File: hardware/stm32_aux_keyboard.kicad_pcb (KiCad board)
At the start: 2 copper layers, 95 x 95 mm, 189 parts, among them J1 I2C_HEADER,2.54, J2 WS2812_HEADER, J3 BUZZER_HEADER, J4 ROT_ENC_HEADER, J5 SWD_SWD, J6 SWD_SWD, J7 ROT_ENC_HEADER, J8 I2C_HEADER,2.54, Q1 SS9013_J3, SW1 USR_BTN_1, SW10 KEY22, SW11 KEY23, SW12 KEY31, SW13 KEY32, SW14 KEY33, SW18 ROT1, SW19 SW_RESET,2_leg,SMD, SW2 USR_BTN_2, SW3 USR_BTN_3, SW5 ROT2, SW6 KEY11, SW7 KEY12, SW8 KEY13, SW9 KEY21, U1 SSD1306-OLED-I2C, U10 STM32F103C8T6, U2 AMS1117-3.3, U3 74AHCT1G125, U4 USB, U5 USBLC6-2SC6_SOT23-6, U6 STM32F103C8T6_rect, U7 SWD, U8 AMS1117-3.3, U9 USBLC6-2SC6_SOT23-6, Y1 O_8M, Y2 O8M, Y3 O32.768K

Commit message: update,
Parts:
- removed REF**: test1, casing:test1
- JP7: value B0 -> BOOT0
- JP8: value B1 -> BOOT1
- U5, U9: moved to F.Cu
- moved J1 8.20 mm to (99.2, 99.4)
- moved U9 7.69 mm to (82.3, 28.1), turned to 90 degrees
- moved RN4 7.02 mm to (82.6, 29.6), turned to 270 degrees
- moved R2 4.70 mm to (104.0, 95.7), turned to 270 degrees
- moved U5 4.69 mm to (88.2, 29.5), turned to 270 degrees
- moved TP8 2.70 mm to (85.8, 32.5)
- moved R1 2.30 mm to (106.0, 95.7), turned to 270 degrees
- renumbered VUSB1 to VUSB1_HEALTHY1
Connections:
- RN4 pad 1: Net-(RN4-Pad1) -> Net-(R27-Pad2)
- RN4 pad 2: Net-(R27-Pad2) -> Net-(RN4-Pad2)
- RN4 pad 7: /stm32_swd/USB_P -> /stm32_swd/USB_N
- RN4 pad 8: /stm32_swd/USB_N -> /stm32_swd/USB_P
- U9 pad 4: Net-(RN4-Pad1) -> Net-(RN4-Pad2)
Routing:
- net Vusb: track 44.9 -> 14.2 mm, vias 4 -> 3
- net /oled/SCL: track 108.4 -> 86.2 mm, vias 1 -> 4
- net /oled/SDA: track 77.6 -> 88.6 mm, vias 3 -> 4
- net Net-(RN4-Pad1): track 9.28 -> 0.99 mm
- net Net-(U7-Pad3): track 19.2 -> 11.5 mm, vias 1 -> 2
- net /stm32_swd/USB_P: track 59.8 -> 52.8 mm, vias 3 -> 1
- net /stm32_core/USR_BTN3: track 90.8 -> 97.0 mm
- net Voled: track 36.7 -> 41.9 mm
- net Net-(RN1-Pad1): track 11.7 -> 6.92 mm, vias 1 -> 0
- net /stm32_swd/USB_N: track 55.2 -> 50.5 mm, vias 3 -> 1
- net Net-(JP8-Pad2): track 35.7 -> 31.8 mm
- net VCC: track 407.5 -> 411.2 mm
- net Net-(RN4-Pad2): track 0.00 -> 3.50 mm, vias 0 -> 1
- net Net-(U7-Pad2): track 15.2 -> 12.2 mm, vias 1 -> 2
- net Net-(RN1-Pad2): track 8.24 -> 11.1 mm, vias 1 -> 0
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
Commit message: update,
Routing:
- net GND: track 984.0 -> 990.1 mm
- net VCC: track 411.2 -> 406.6 mm, vias 8 -> 9
- net Net-(R27-Pad2): track 12.2 -> 15.5 mm, vias 1 -> 2
- net Vstm32_stlink: track 172.1 -> 172.9 mm

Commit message: update,
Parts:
- JP5, JP6, R25, R5, R6: moved to B.Cu
- moved RN1 6.00 mm to (91.9, 29.1), turned to 0 degrees
- moved R25 4.63 mm to (93.5, 32.1), turned to 180 degrees
- moved R22 4.17 mm to (103.0, 36.0), turned to 0 degrees
- moved R23 4.06 mm to (103.0, 34.0), turned to 180 degrees
- moved JP6 4.00 mm to (109.1, 36.4)
- moved JP5 3.93 mm to (106.5, 36.4)
- moved R26 3.76 mm to (74.4, 25.4)
- moved C31 3.10 mm to (98.9, 40.7)
- moved C32 3.10 mm to (96.9, 44.7)
- moved C33 3.10 mm to (96.9, 47.7)
- moved C34 3.10 mm to (105.4, 42.7)
- moved C35 3.10 mm to (103.7, 49.2)
- moved R19 3.10 mm to (96.9, 43.2)
- moved R20 3.10 mm to (100.9, 40.7)
- moved R21 3.10 mm to (96.9, 46.2)
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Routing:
- net /stm32_core/USB_P: track 76.7 -> 141.7 mm, vias 4 -> 2
- net Vusb: track 14.2 -> 48.6 mm, vias 3 -> 5
- net /stm32_swd/T_JTMS: track 19.8 -> 53.4 mm, vias 1 -> 5
- net GND: track 990.1 -> 963.2 mm, vias 9 -> 12
- net /stm32_swd/T_JTCK: track 19.2 -> 40.4 mm, vias 1 -> 3
- net /stm32_swd/D_SWDIO: track 62.7 -> 83.6 mm, vias 1 -> 2
- net /stm32_swd/USB_N: track 50.5 -> 65.4 mm, vias 1 -> 3
- net /stm32_swd/D_SWCLK: track 51.1 -> 65.0 mm, vias 1 -> 3
- net Net-(D25-Pad1): track 13.5 -> 3.47 mm
- net /oled/SCL: track 86.2 -> 94.7 mm, vias 4 -> 5
- net /oled/SDA: track 88.6 -> 80.1 mm, vias 4 -> 5
- net /keyboard_key/COL3: track 79.8 -> 88.0 mm, vias 3 -> 5
- net /stm32_swd/USB_P: track 52.8 -> 45.1 mm, vias 1 -> 3
- net Net-(RN1-Pad2): track 11.1 -> 3.53 mm
- net Vstm32_stlink: track 172.9 -> 165.5 mm
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
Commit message: update for autoroute complete,
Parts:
- moved R23 1.50 mm to (103.1, 32.5)
- moved JP6 1.10 mm to (110.2, 36.5)
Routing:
- net GND: track 963.2 -> 885.7 mm, vias 12 -> 5
- net /stm32_core/USB_P: track 141.7 -> 70.4 mm, vias 2 -> 0
- net /stm32_core/BOOT1: track 81.2 -> 22.3 mm, vias 0 -> 2
- net /status_display/USR_LED_2: track 101.2 -> 150.1 mm, vias 4 -> 0
- net /status_display/USR_LED_1: track 88.8 -> 130.5 mm, vias 2 -> 0
- net /keyboard_key/ROW2: track 86.6 -> 125.4 mm
- net /stm32_swd/T_JTMS: track 53.4 -> 18.4 mm, vias 5 -> 1
- net /stm32_swd/USB_N: track 65.4 -> 34.0 mm, vias 3 -> 1
- net /stm32_swd/T_JTCK: track 40.4 -> 12.5 mm, vias 3 -> 1
- net /stm32_core/USB_N: track 79.5 -> 54.3 mm, vias 3 -> 2
- net /oled/SCL: track 94.7 -> 72.9 mm, vias 5 -> 0
- net VCC: track 409.2 -> 387.6 mm, vias 9 -> 6
- net /WS2812/WS2812_IN: track 170.4 -> 191.4 mm, vias 2 -> 1
- net /stm32_core/PC13: track 29.3 -> 9.72 mm
- net +3V3: track 249.7 -> 269.1 mm, vias 3 -> 1
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
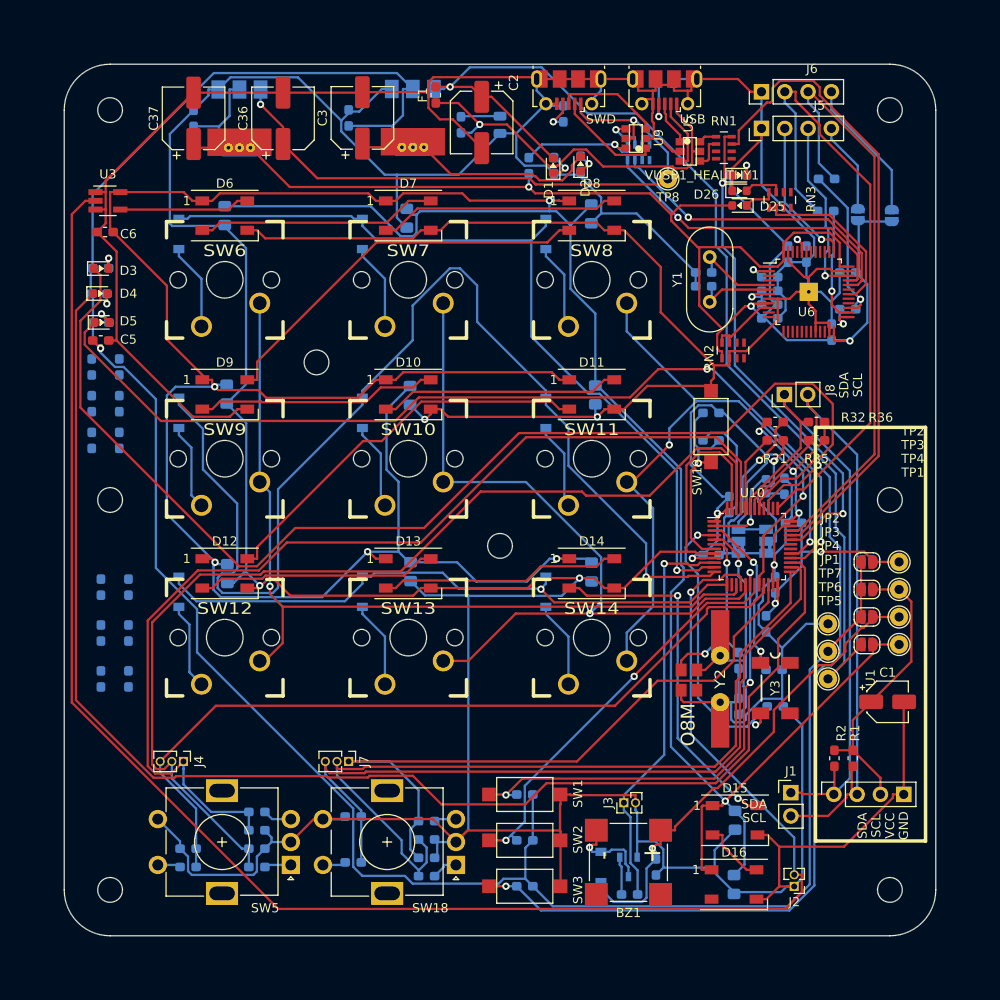
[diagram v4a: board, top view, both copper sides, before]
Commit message: update for tidy tracks,
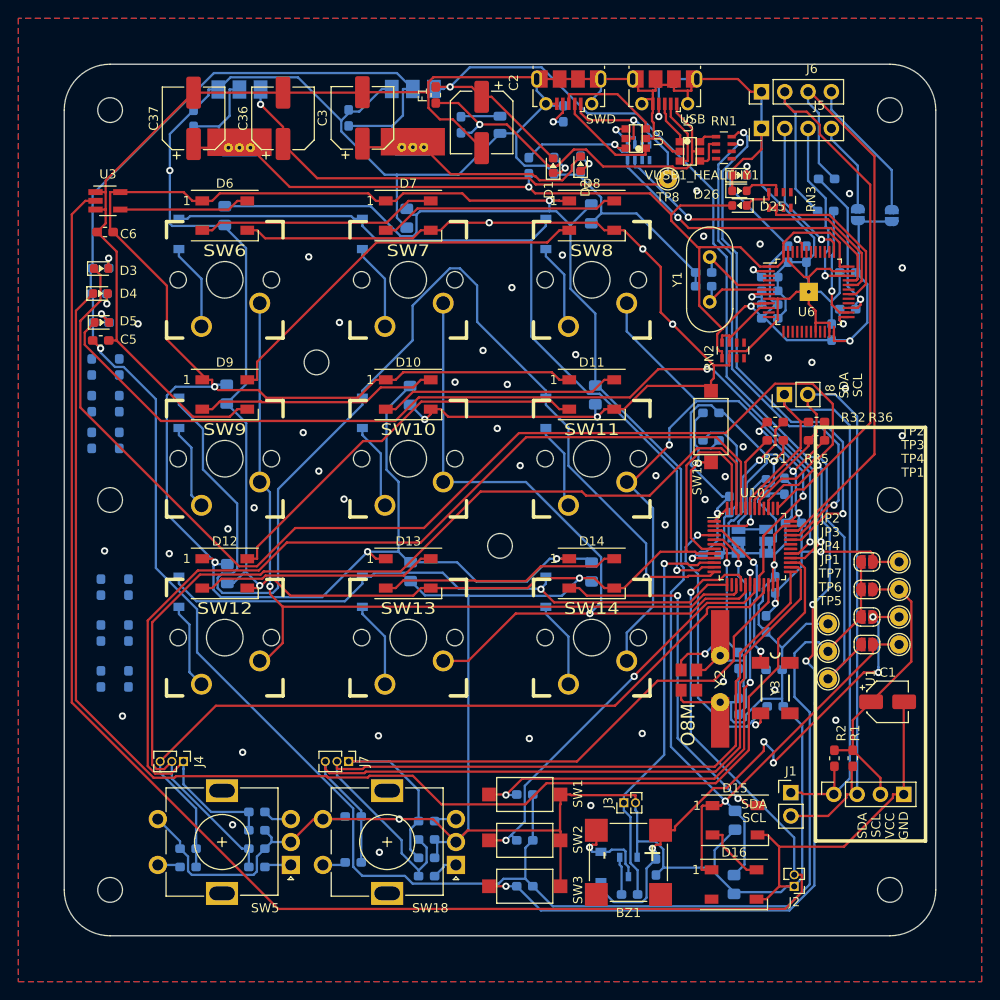
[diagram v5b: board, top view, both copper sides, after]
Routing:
- net /stm32_core/USB_P: track 70.4 -> 55.2 mm, vias 0 -> 2
- net Vbuzzer: track 52.9 -> 58.6 mm, vias 1 -> 5
- net /stm32_core/USB_N: track 54.3 -> 58.6 mm
- net +3V3: track 269.1 -> 273.3 mm
- net /oled/SDA: track 71.4 -> 74.3 mm
- net /oled/SCL: track 72.9 -> 74.7 mm
- net +5V: track 118.2 -> 118.9 mm
- net /stm32_core/USR_BTN3: track 94.0 -> 93.4 mm, vias 2 -> 4
- net GND: track 885.7 -> 886.2 mm, vias 5 -> 53
- added copper zone on B.Cu, net GND
- added copper zone on F.Cu, net GND

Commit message: update for tidy tracks,
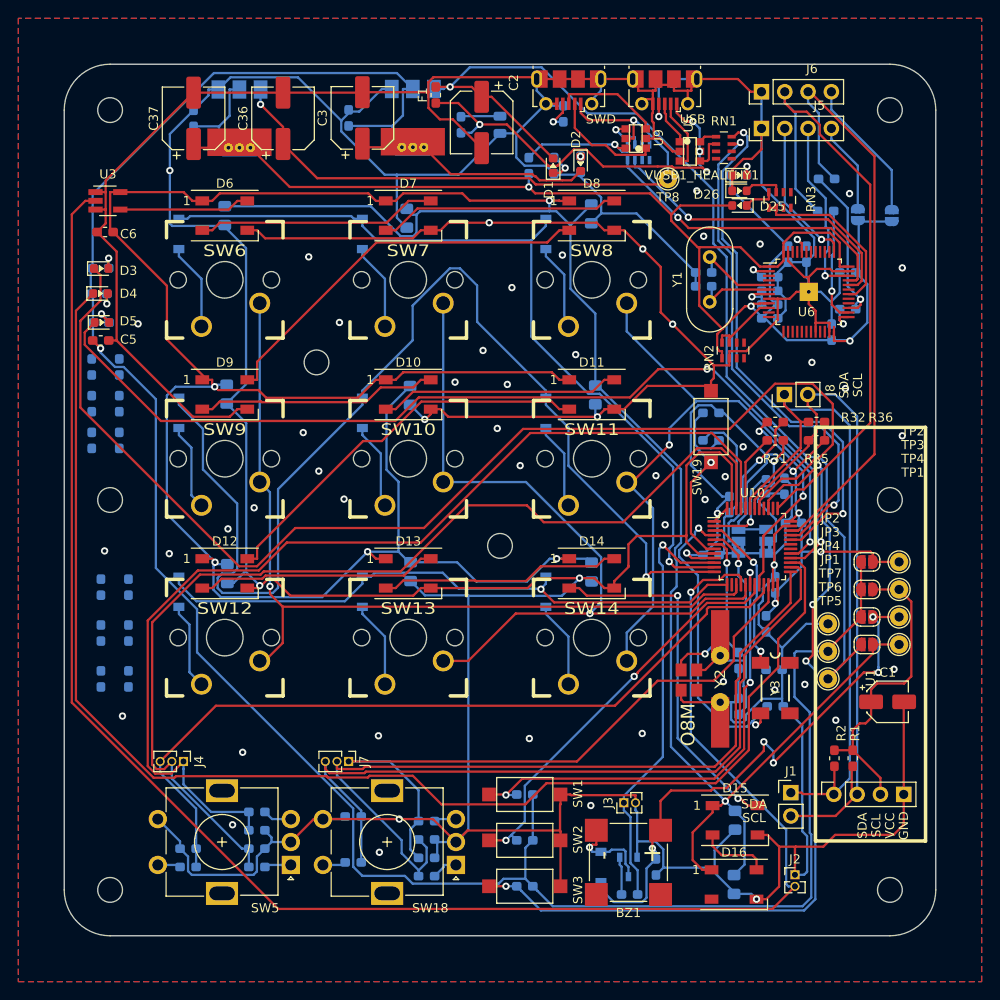
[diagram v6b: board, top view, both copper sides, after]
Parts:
- moved J2 1.27 mm to (99.7, 108.3), turned to 0 degrees
- turned D2 to 270 degrees
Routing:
- net /stm32_core/BUZZER: track 44.1 -> 47.2 mm
- net Vusb: track 43.0 -> 45.8 mm, vias 1 -> 4
- net Net-(D2-Pad1): track 2.47 -> 0.00 mm
- net Voled: track 31.6 -> 33.7 mm
- net /stm32_core/OSC32K_N: track 32.5 -> 34.1 mm
- net Vstm32: track 91.4 -> 92.8 mm
- net Vbuzzer: track 58.6 -> 59.9 mm
- net /rot_enc2/B: track 111.1 -> 112.3 mm
- net /WS2812/WS2812_IN: track 191.4 -> 190.3 mm
- net /stm32_core/USR_BTN3: track 93.4 -> 94.4 mm
- net Net-(U7-Pad2): track 11.4 -> 12.3 mm
- net +3V3: track 273.3 -> 272.5 mm
- net GND: track 886.2 -> 886.9 mm, vias 53 -> 56
- net Net-(D15-Pad2): track 7.04 -> 7.75 mm
- net /stm32_core/RESET: track 21.5 -> 21.0 mm

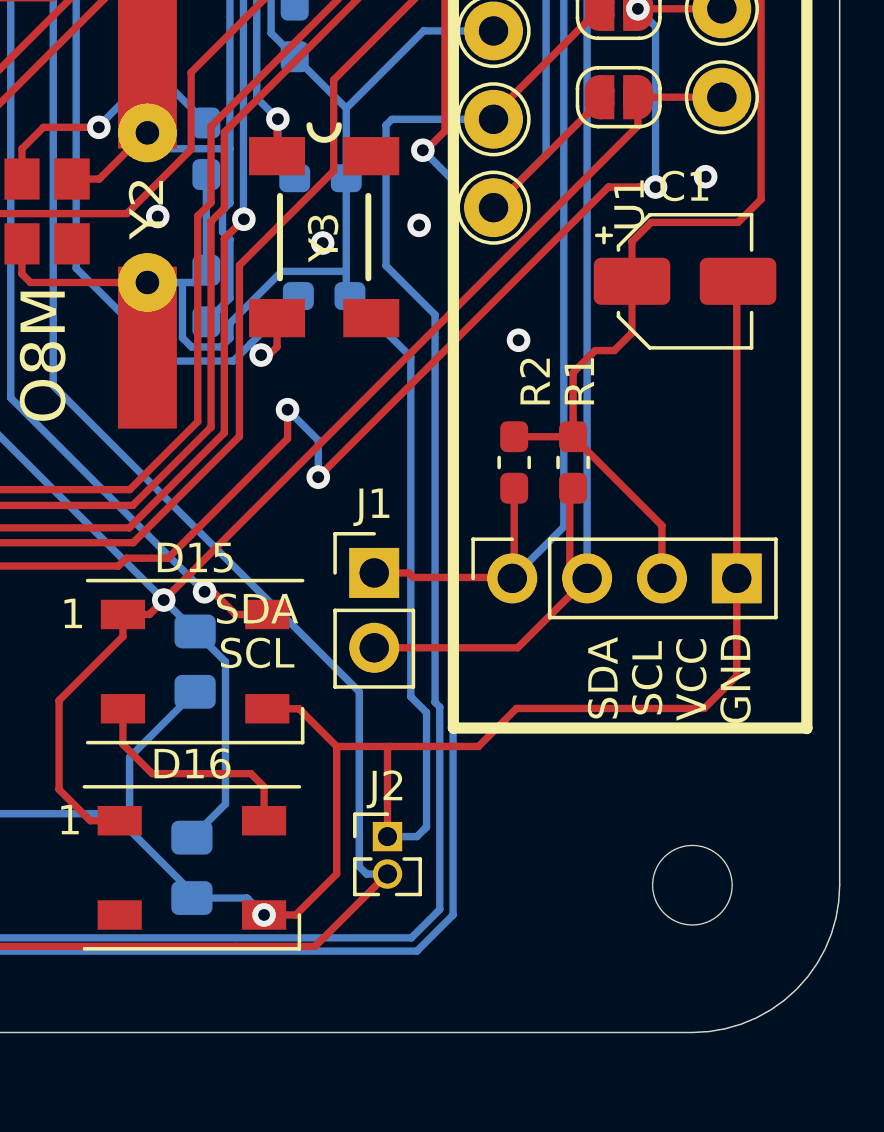
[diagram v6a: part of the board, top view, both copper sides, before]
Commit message: update for tidy tracks,
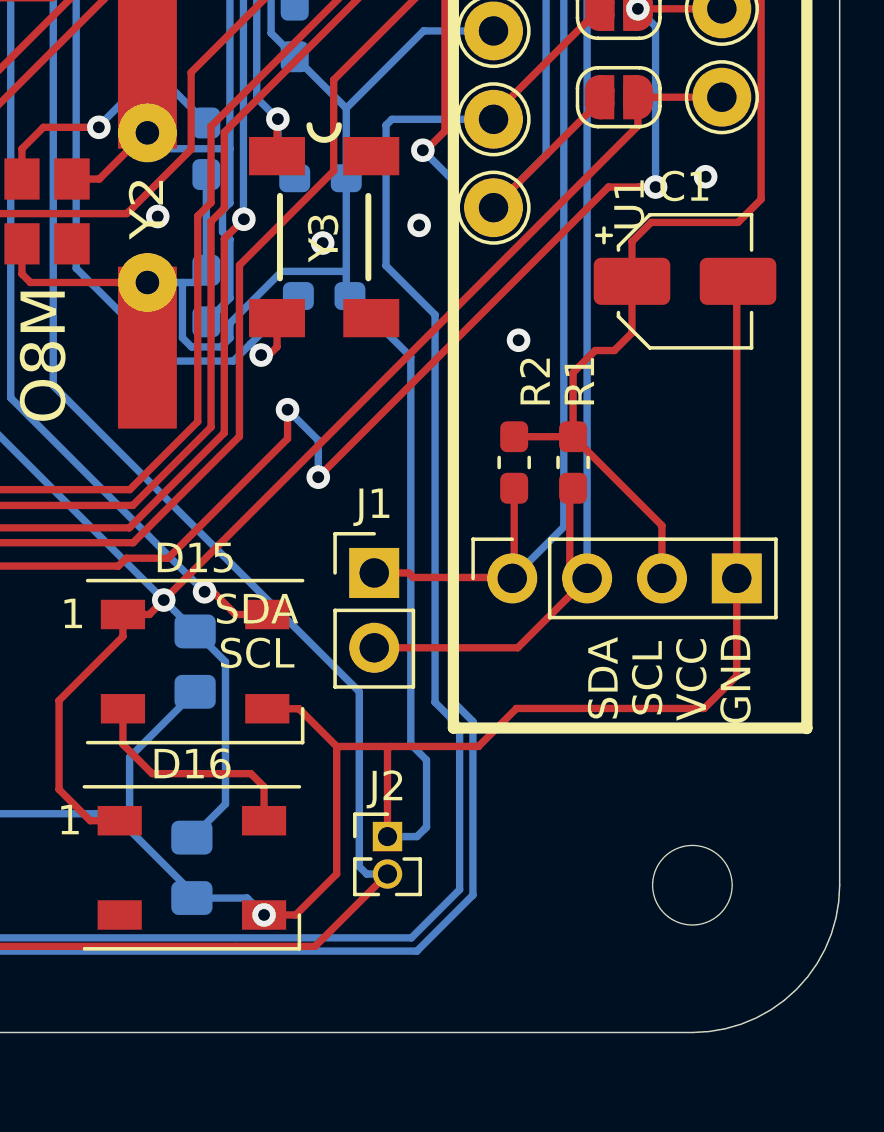
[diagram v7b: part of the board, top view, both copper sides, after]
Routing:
- net +3V3: track 272.5 -> 273.1 mm
- net /stm32_core/USR_BTN3: track 94.4 -> 95.0 mm
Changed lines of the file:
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@@
     (thickness 1.6)
     (drawings 18)
-    (tracks 1801)
+    (tracks 1803)
     (zones 0)
     (modules 188)
@@
   (segment (start 89.094525 73.33) (end 87.8211 72.056575) (width 0.25) (layer F.Cu) (net 1))
   (segment (start 100.975011 108.024989) (end 100.875 108.125) (width 0.25) (layer B.Cu) (net 1))
-  (segment (start 100.975011 104.1386) (end 100.975011 108.024989) (width 0.25) (layer B.Cu) (net 1))
-  (segment (start 100.4416 103.60519) (end 100.975011 104.1386) (width 0.25) (layer B.Cu) (net 1))
-  (segment (start 98.375 90) (end 100.4416 92.0666) (width 0.25) (layer B.Cu) (net 1))
-  (segment (start 100.4416 92.0666) (end 100.4416 103.60519) (width 0.25) (layer B.Cu) (net 1))
   (segment (start 100.65 108.35) (end 100.975011 108.024989) (width 0.25) (layer B.Cu) (net 1))
   (segment (start 99.65 108.35) (end 100.65 108.35) (width 0.25) (layer B.Cu) (net 1))
@@
   (segment (start 93.01 110.435) (end 94.885 110.435) (width 0.25) (layer B.Cu) (net 1))
   (segment (start 94.885 110.435) (end 95.46 111.01) (width 0.25) (layer B.Cu) (net 1))
+  (segment (start 100.975011 105.750011) (end 100.975011 108.024989) (width 0.25) (layer B.Cu) (net 1))
+  (segment (start 100.4416 105.2166) (end 100.975011 105.750011) (width 0.25) (layer B.Cu) (net 1))
+  (segment (start 98.375 90) (end 100.4416 92.0666) (width 0.25) (layer B.Cu) (net 1))
+  (segment (start 100.4416 92.0666) (end 100.4416 105.2166) (width 0.25) (layer B.Cu) (net 1))
   (segment (start 86.1643 36.3852) (end 87.1495 35.4) (width 0.25) (layer F.Cu) (net 2))
   (segment (start 87.1495 35.4) (end 92.8125 35.4) (width 0.25) (layer F.Cu) (net 2))
@@
   (segment (start 74.2898 32.6532) (end 75.2743 32.6532) (width 0.25) (layer F.Cu) (net 30))
   (segment (start 71.574072 110.099072) (end 71.075 109.6) (width 0.25) (layer B.Cu) (net 30))
-  (segment (start 101.264 103.791178) (end 101.425022 103.9522) (width 0.25) (layer B.Cu) (net 30))
-  (segment (start 101.264 90.636) (end 101.264 103.791178) (width 0.25) (layer B.Cu) (net 30))
   (segment (start 73.262 111.787) (end 71.574072 110.099072) (width 0.25) (layer B.Cu) (net 30))
+  (segment (start 100.463 111.787) (end 73.262 111.787) (width 0.25) (layer B.Cu) (net 30))
+  (segment (start 99.6 88.972) (end 101.264 90.636) (width 0.25) (layer B.Cu) (net 30))
   (segment (start 103.25 84) (end 99.8 84) (width 0.25) (layer B.Cu) (net 30))
-  (segment (start 101.425022 103.9522) (end 101.425022 110.824978) (width 0.25) (layer B.Cu) (net 30))
+  (segment (start 102.1 110.15) (end 100.463 111.787) (width 0.25) (layer B.Cu) (net 30))
   (segment (start 99.6 84.2) (end 99.6 88.972) (width 0.25) (layer B.Cu) (net 30))
   (segment (start 99.8 84) (end 99.6 84.2) (width 0.25) (layer B.Cu) (net 30))
-  (segment (start 101.425022 110.824978) (end 100.463 111.787) (width 0.25) (layer B.Cu) (net 30))
-  (segment (start 99.6 88.972) (end 101.264 90.636) (width 0.25) (layer B.Cu) (net 30))
-  (segment (start 100.463 111.787) (end 73.262 111.787) (width 0.25) (layer B.Cu) (net 30))
+  (segment (start 102.1 104.627178) (end 102.1 110.15) (width 0.25) (layer B.Cu) (net 30))
+  (segment (start 101.264 90.636) (end 101.264 103.791178) (width 0.25) (layer B.Cu) (net 30))
+  (segment (start 101.264 103.791178) (end 102.1 104.627178) (width 0.25) (layer B.Cu) (net 30))
   (segment (start 33 96) (end 33 96.8253) (width 0.25) (layer B.Cu) (net 31))
   (segment (start 33 96.8253) (end 33 98.4942) (width 0.25) (layer B.Cu) (net 31))
@@
   (segment (start 102.55 69.7154) (end 103.4423 70.6077) (width 0.25) (layer B.Cu) (net 50))
   (segment (start 102.55 64.0965) (end 102.55 69.7154) (width 0.25) (layer B.Cu) (net 50))
-  (segment (start 101.875033 86.075033) (end 101.875033 111.011378) (width 0.25) (layer B.Cu) (net 50))
-  (segment (start 100.649111 112.2373) (end 71.9623 112.2373) (width 0.25) (layer B.Cu) (net 50))
   (segment (start 69.824072 110.099072) (end 69.325 109.6) (width 0.25) (layer B.Cu) (net 50))
-  (segment (start 101.875033 111.011378) (end 100.649111 112.2373) (width 0.25) (layer B.Cu) (net 50))
   (segment (start 71.9623 112.2373) (end 69.824072 110.099072) (width 0.25) (layer B.Cu) (net 50))
+  (segment (start 101.875033 86.075033) (end 101.875033 103.7658) (width 0.25) (layer B.Cu) (net 50))
+  (segment (start 102.550011 110.3364) (end 100.649111 112.2373) (width 0.25) (layer B.Cu) (net 50))
+  (segment (start 100.649111 112.2373) (end 71.9623 112.2373) (width 0.25) (layer B.Cu) (net 50))
+  (segment (start 101.875033 103.7658) (end 102.550011 104.440778) (width 0.25) (layer B.Cu) (net 50))
   (segment (start 100.85 85.05) (end 101.875033 86.075033) (width 0.25) (layer B.Cu) (net 50))
+  (segment (start 102.550011 104.440778) (end 102.550011 110.3364) (width 0.25) (layer B.Cu) (net 50))
   (segment (start 84.81 25.7008) (end 84.81 24.3125) (width 0.25) (layer F.Cu) (net 51))
   (segment (start 84.625 22.1) (end 84.81 22.285) (width 0.25) (layer B.Cu) (net 51))
